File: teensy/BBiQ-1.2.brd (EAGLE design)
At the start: 61.5 x 58.1 mm, 29 parts, among them IC1 ESP-WROOM-02, J1 MJ-2506N, J2 MJ-2506N, J3 MJ-2506N, J4 MJ-2506N, T1 2N3904

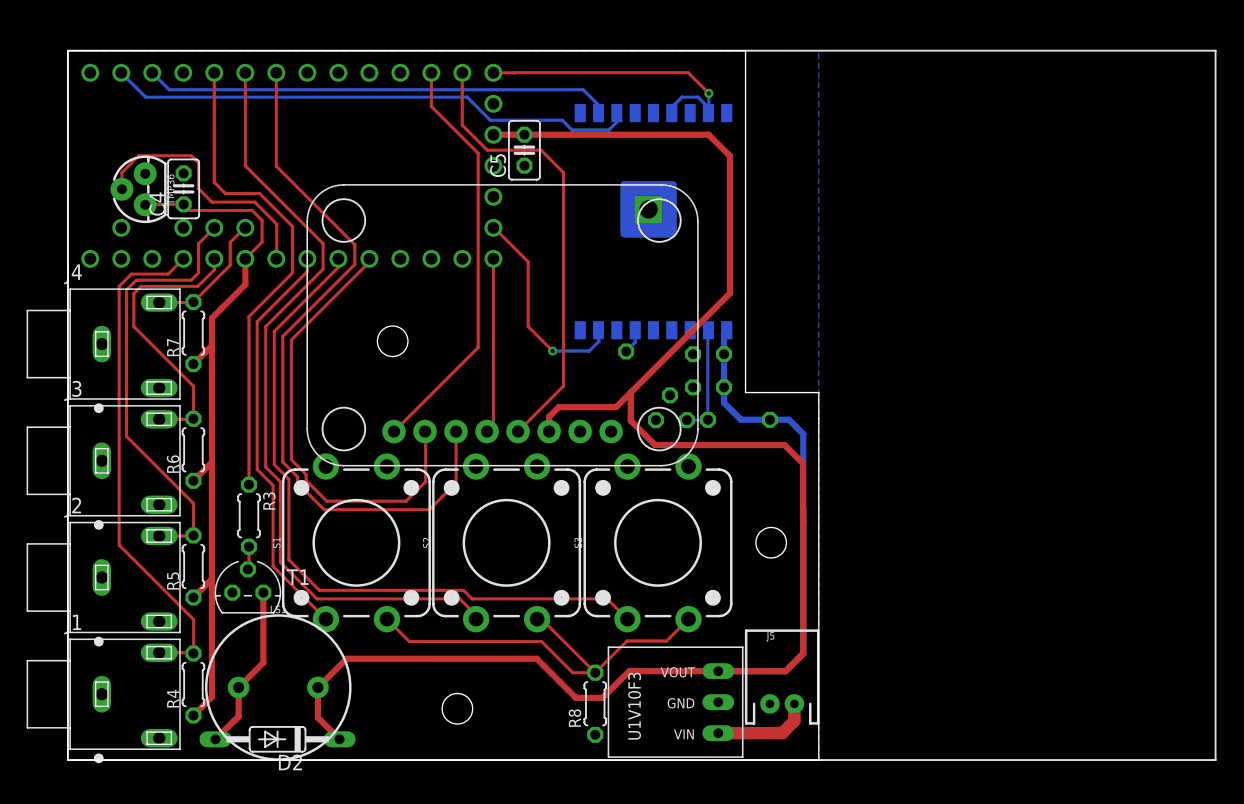
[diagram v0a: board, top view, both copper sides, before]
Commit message: new board with teensyview
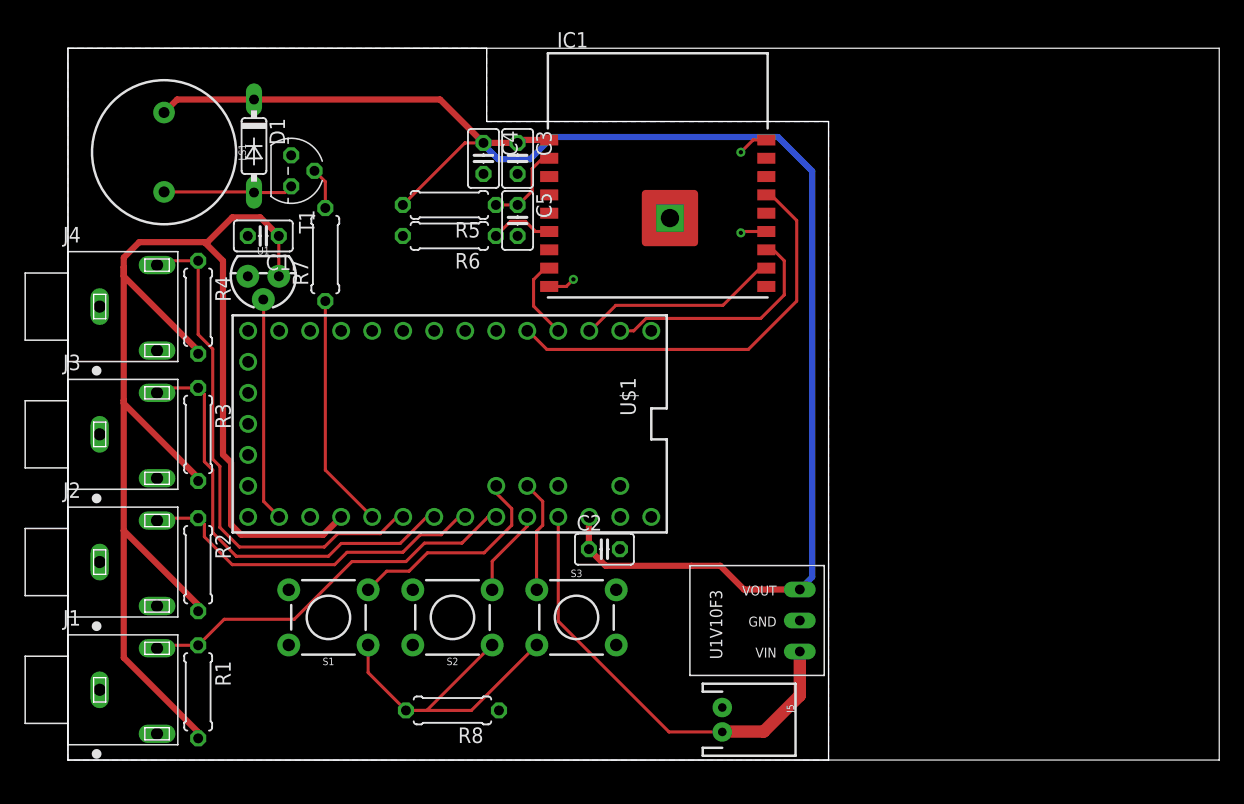
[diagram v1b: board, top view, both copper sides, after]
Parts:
- removed D2: 1N4148DO35-10, diode:DO35-10
- removed OLED1: ADAFRUIT_128X32_SPI_OLED, Adafruit OLED 128x32 Mono:ADAFRUIT_128X32_SPI_OLED
- removed TMP36: (no value), SparkFun-Sensors:TO-92
- added D1: 1N4148, diode:DO35-7
- added U1: (no value), SparkFun-Sensors:TO-92
- C1: value 10µF -> 0.1µF
- C4: value 0.1µF -> 10µF
- R1, R2, R3: value 10kΩ -> 10k 1%; device resistor:0204/5 -> resistor:0207/7
- R4: value 10kΩ 1% -> 10k 1%; device resistor:0204/5 -> resistor:0207/7
- R5, R6, R7: value 10kΩ 1% -> 10kΩ; device resistor:0204/5 -> resistor:0207/7
- R8: value 1kΩ -> 10k 1%; device resistor:0204/5 -> resistor:0207/7
- S1, S2, S3: value MOMENTARY-SWITCH-SPST-PTH-12MM -> (none); device SparkFun-Switches:TACTILE_SWITCH_PTH_12MM -> SparkFun-Switches:TACTILE_SWITCH_PTH_6.0MM
- U$1: value U1V10F3 -> TEENSY_LC_ALL_PINS; device U1V10F3:U1V10F3 -> Teensy_3_and_LC_Series_Boards_v1.4:TEENSY_3.0-3.2&LC_ALL_PINS
- U$2: value TEENSY_LC_ALL_PINS -> U1V10F3; device Teensy_3_and_LC_Series_Boards_v1.4:TEENSY_3.0-3.2&LC_ALL_PINS -> U1V10F3:U1V10F3
- moved U$2 55.8 mm to (59.9, 11.4), flipped to the top, turned to 90 degrees
- moved R1 49.6 mm to (10.7, 5.59), flipped to the top, turned to 270 degrees
- moved LS1 44.8 mm to (7.87, 49.8), turned to 270 degrees
- moved R2 40.0 mm to (10.7, 16.0), flipped to the top, turned to 270 degrees
- moved C1 38.5 mm to (16.0, 42.9), flipped to the top, turned to 180 degrees
- moved R5 36.3 mm to (31.2, 45.5), turned to 180 degrees
- moved T1 34.7 mm to (18.3, 48.3), turned to 270 degrees
- moved U$1 31.7 mm to (31.3, 27.5), turned to 270 degrees
- moved R4 30.9 mm to (10.7, 37.1), turned to 270 degrees
- moved R6 27.3 mm to (31.2, 42.9), turned to 180 degrees
- moved C3 24.9 mm to (36.8, 49.3), flipped to the top, turned to 270 degrees
- moved C4 24.7 mm to (34.0, 49.3), turned to 270 degrees
- moved C2 18.1 mm to (43.9, 17.3), flipped to the top
- moved R7 12.6 mm to (21.1, 41.4)
- moved R8 11.7 mm to (31.5, 4.06), turned to 180 degrees
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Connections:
- removed net 3V3O: OLED1.7
- removed net BUTTON_0: S1.3, S1.4, U$2.19/A5
- removed net ESP_LOAD: IC1.8, U$2.RESET/DAC
- removed net N$6: D2.A, LS1.-, T1.1
- removed net N$7: R8.2, S1.1, S1.2, S2.1, S2.2, S3.1, S3.2
- removed net OLED_CK: OLED1.4, U$2.13
- removed net PROBE_0: J1.2, R4.2, U$2.23/A9
- removed net TMP36: TMP36.2, U$2.20/A6
- new net 26/A12/DAC: U$1.RESET/DAC
- new net BUTTON_3: S3.1, U$1.A10
- new net ESP_EN: C5.1, IC1.2, R5.1
- new net ESP_PRG: IC1.8, U$1.2
- new net INT_TEMP: U$1.14/A0, U1.2
- new net N$1: IC1.6, R6.1
- new net OLED_SCLK: U$1.13
- new net PROBE_4: J1.2, R1.1, U$1.21/A7
- net +3V3: now also C3.1, C4.1, D1.C, LS1.-, R5.2, U$1.3.3V, U$1.3.3V1, U$2.VOUT; no longer C1.1, C5.2, D2.C, LS1.+, OLED1.6, R1.2, U$1.VOUT, U$2.3.3V, U$2.3.3V1
- net AREF: now also U$1.AREF; no longer U$2.AREF
- net BUTTON_1: now also S1.3, U$1.A11; no longer S2.3, S2.4, U$2.4
- net BUTTON_2: now also S2.3, U$1.22/A8; no longer S3.3, S3.4, U$2.18/A4
- net BUZZER: now also R7.1, U$1.17/A3; no longer R3.1, U$2.3
- net ESP_RST: now also U$1.3; no longer IC1.17, U$2.12
- net ESP_RX: now also U$1.1; no longer U$2.1
- net ESP_TX: now also U$1.0; no longer U$2.0
- net GND: now also C3.2, C5.2, R6.2, U$1.AGND, U$1.GND1, U1.3; no longer C3.1, C5.1, J3.1, OLED1.8, R2.1, TMP36.3, U$2.AGND, U$2.GND1
- net N$2: now also R7.2, T1.2; no longer C3.2, IC1.2, R1.1
- net N$3: now also D1.A, LS1.+, T1.1; no longer IC1.6, R2.2
- net N$4: now also R8.2, S1.1, S2.1, S3.3; no longer R3.2, T1.2
- net OLED_CS: now also U$1.10; no longer OLED1.1, U$2.10
- net OLED_DATA: now also U$1.11; no longer OLED1.5, U$2.11
- net OLED_DC: now also U$1.5; no longer OLED1.3, U$2.5
- net OLED_RST: now also U$1.15/A1; no longer OLED1.2, U$2.17/A3
- net PROBE_1: now also J4.2, R4.1, U$1.18/A4; no longer J2.2, R5.2, U$2.A10
- net PROBE_2: now also R3.1, U$1.19/A5; no longer R6.2, U$2.22/A8
- net PROBE_3: now also J2.2, R2.1, U$1.20/A6; no longer J4.2, R7.2, U$2.A11
- net PROBE_PWR: now also C1.1, R1.2, R2.2, R3.2, R4.2, U$1.16/A2, U1.1; no longer C4.1, R4.1, R5.1, R6.1, R7.1, TMP36.1, U$2.21/A7
- net VBAT: now also U$1.23/A9, U$2.VIN; no longer U$1.VIN
- net VIN: now also U$1.VIN; no longer U$2.VIN
- net VUSB: now also U$1.VUSB; no longer U$2.VUSB
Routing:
- net PROBE_PWR: track 59.7 -> 121.8 mm
- net OLED_DC: track 58.2 -> 0.00 mm
- net BUTTON_2: track 57.1 -> 7.16 mm
- net +3V3: track 173.8 -> 127.7 mm
- net BUTTON_1: track 63.3 -> 17.7 mm
- net PROBE_0: track 41.6 -> 0.00 mm
- net OLED_DATA: track 37.0 -> 0.00 mm
- net OLED_RST: track 36.6 -> 0.00 mm
- net N$7: track 34.9 -> 0.00 mm
- net OLED_CS: track 33.8 -> 0.00 mm
- net BUTTON_0: track 33.5 -> 0.00 mm
- net PROBE_4: track 0.00 -> 32.2 mm
- net VBAT: track 8.04 -> 36.9 mm
- net N$4: track 1.89 -> 28.9 mm
- net ESP_TX: track 43.5 -> 19.3 mm
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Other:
- board size 61.5 x 58.1 mm -> 62.3 x 58.3 mm

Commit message: tweaks
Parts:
- added C6: 1000µF, resistor:E3,5-8
- added U$3, U$4, U$5, U$6: MOUNTINGHOLE2.5, microbuilder:MOUNTINGHOLE_2.5_PLATED
- C4: device resistor:C025-025X050 -> resistor:E2-5
- moved U$2 2.03 mm to (59.9, 13.5)
- moved J5 1.83 mm to (52.6, 4.83)
- moved C4 1.78 mm to (32.3, 49.3)
- moved R6 0.57 mm to (30.7, 42.7)
- moved R5 0.57 mm to (30.7, 45.2)
- moved C3 0.25 mm to (36.8, 49.0)
- moved C5 0.25 mm to (36.8, 43.9)
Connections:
- net +3V3: now also C4.+, C6.+; no longer C4.1
- net GND: now also C4.-, C6.-; no longer C4.2
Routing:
- net +3V3: track 127.7 -> 131.7 mm
- net ESP_EN: track 7.03 -> 7.75 mm
- net N$1: track 5.20 -> 5.82 mm
